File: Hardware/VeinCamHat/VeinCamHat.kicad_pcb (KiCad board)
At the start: 2 copper layers, 65 x 56 mm, 65 parts, among them J1 10118193-0001LF, J2 Raspberry_Pi_2_3, Q1 BSD235N, Q2 MMUN2133L, SW1 SS-12D07-VG 4, U1 MCP3021, U2 TPS61092, U3 MCP73871

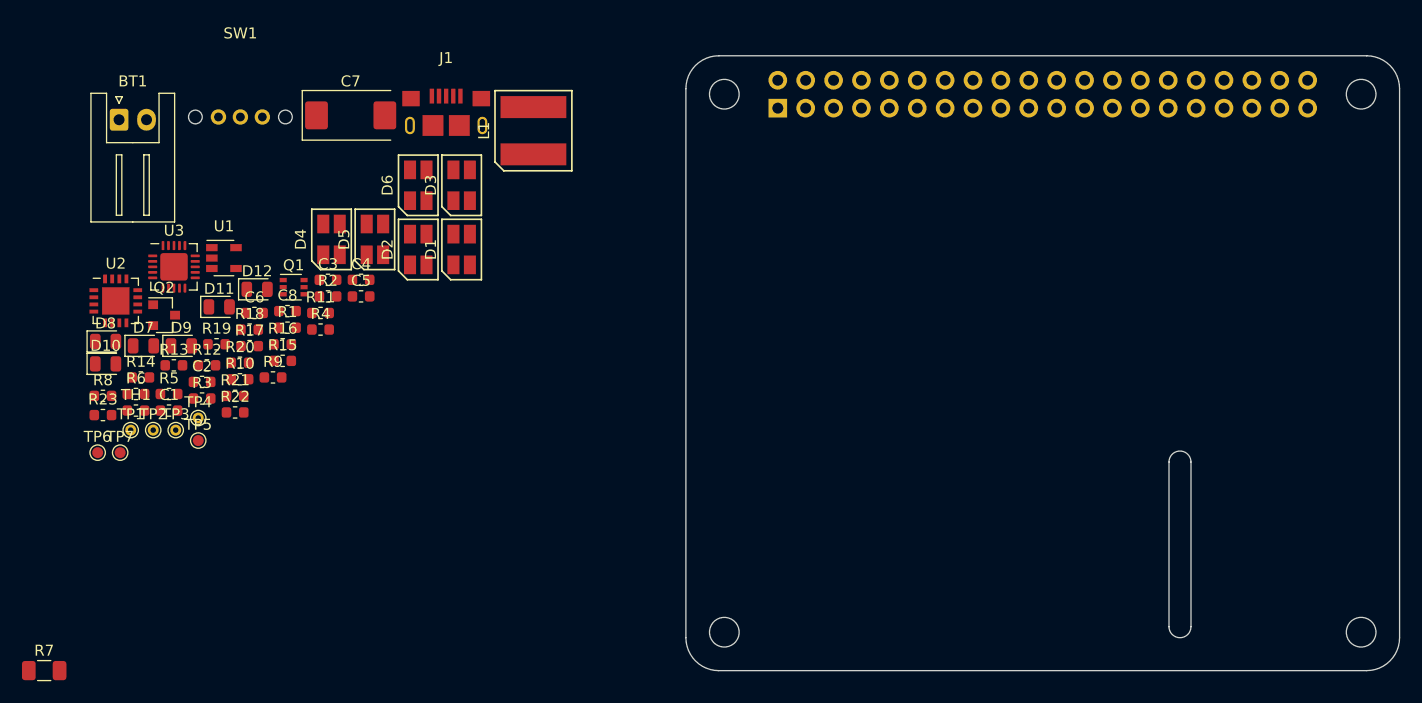
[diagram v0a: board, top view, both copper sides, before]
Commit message: Changed plans for VeinCam Plus, both boards laid out
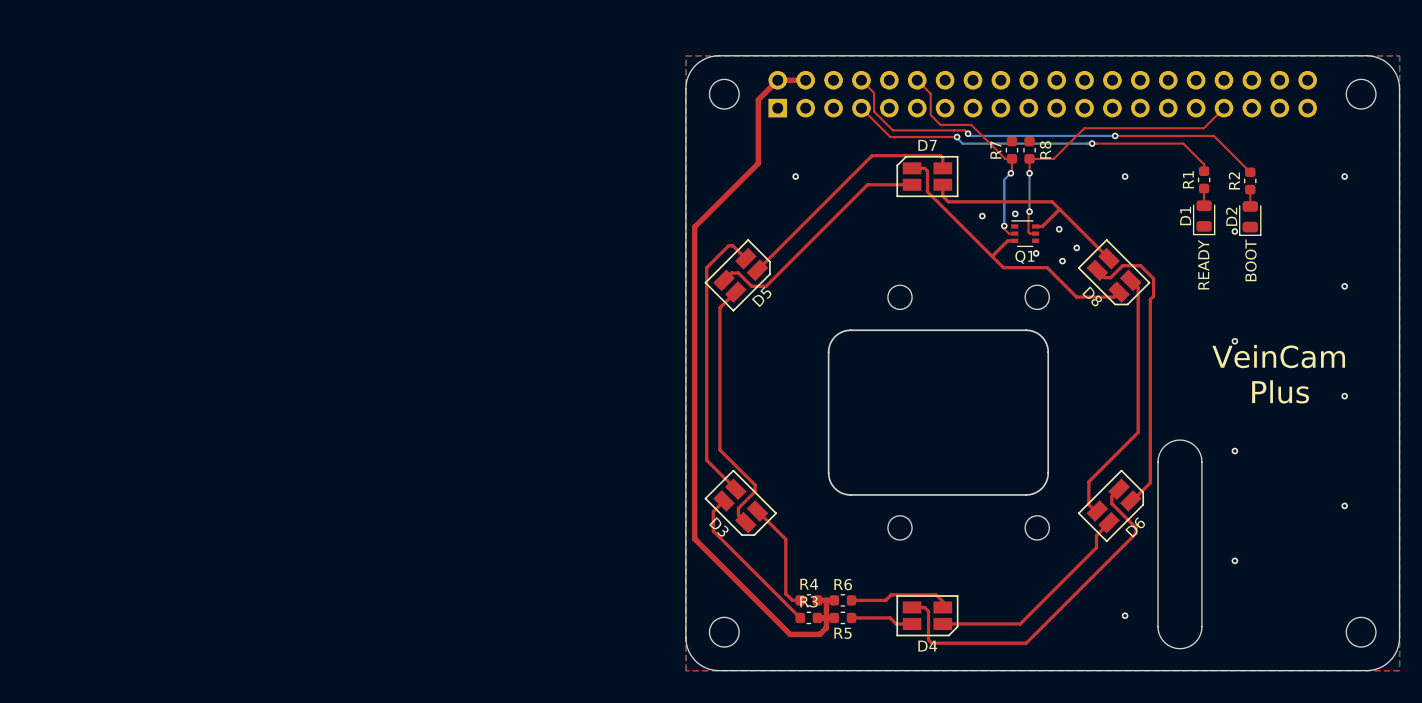
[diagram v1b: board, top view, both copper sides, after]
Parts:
- removed BT1: 3v7 LIPO, Connector_JST:JST_XH_S02B-XH-A_1x02_P2.50mm_Horizontal
- removed C1, C3, C4, C8: 10u, Capacitor_SMD:C_0603_1608Metric
- removed C2, C5: 100n, Capacitor_SMD:C_0603_1608Metric
- removed C6: 2u2, Capacitor_SMD:C_0603_1608Metric
- removed C7: 100u, Capacitor_Tantalum_SMD:CP_EIA-7343-31_Kemet-D
- removed D10, D12: RED LED, LED_SMD:LED_0805_2012Metric
- removed D11, D9: GREEN LED, LED_SMD:LED_0805_2012Metric
- removed J2: Raspberry_Pi_2_3, Connector_PinSocket_2.54mm:PinSocket_2x20_P2.54mm_Vertical
- removed L1: SRN6045-6R8Y, VeinCam_Footprints:SRN6045
- removed Q2: MMUN2133L, Package_TO_SOT_SMD:SOT-23
- removed R10, R14, R9: 10k, Resistor_SMD:R_0603_1608Metric
- removed R11, R12, R13, R15, R16, R21, R23: 1k, Resistor_SMD:R_0603_1608Metric
- removed R17: 1M87, Resistor_SMD:R_0603_1608Metric
- removed R18: 340k, Resistor_SMD:R_0603_1608Metric
- removed R19: 270k, Resistor_SMD:R_0603_1608Metric
- removed R20, R22: 100k, Resistor_SMD:R_0603_1608Metric
- removed SW1: SS-12D07-VG 4, VeinCam_Footprints:SS-12D07-VG4
- removed TH1: 10k NTC, Resistor_SMD:R_0603_1608Metric
- removed TP2, TP3, TP4: TestPoint, TestPoint:TestPoint_THTPad_D1.0mm_Drill0.5mm
- removed TP5: TP_BATT, TestPoint:TestPoint_Pad_D1.0mm
- removed TP6: TP_5V0, TestPoint:TestPoint_Pad_D1.0mm
- removed TP7: TP_VLIPO, TestPoint:TestPoint_Pad_D1.0mm
- removed U1: MCP3021, Package_TO_SOT_SMD:SOT-23-5
- removed U2: TPS61092, Package_DFN_QFN:QFN-16-1EP_4x4mm_P0.65mm_EP2.5x2.5mm
- removed U3: MCP73871, Package_DFN_QFN:QFN-20-1EP_4x4mm_P0.5mm_EP2.5x2.5mm
- D1: value SFH7252 -> GREEN LED; footprint VeinCam_Footprints:SFH7252 -> LED_SMD:LED_0805_2012Metric
- D2: value SFH7252 -> RED LED; footprint VeinCam_Footprints:SFH7252 -> LED_SMD:LED_0805_2012Metric
- D7: value GREEN LED -> SFH7252; footprint LED_SMD:LED_0805_2012Metric -> VeinCam_Footprints:SFH7252
- D8: value RED LED -> SFH7252; footprint LED_SMD:LED_0805_2012Metric -> VeinCam_Footprints:SFH7252
- J1: value 10118193-0001LF -> Raspberry_Pi_2_3; footprint VeinCam_Footprints:10118193-0001LF -> Connector_PinSocket_2.54mm:PinSocket_2x20_P2.54mm_Vertical; moved to B.Cu
- R1: value 0R0 -> 1k
- R2: value DNP -> 1k
- R7: value DNP -> 10k; footprint Resistor_SMD:R_1206_3216Metric -> Resistor_SMD:R_0603_1608Metric
- TP1: value TestPoint -> Camera Outline; footprint TestPoint:TestPoint_THTPad_D1.0mm_Drill0.5mm -> VeinCam_Footprints:PiCamera
- moved R7 100.1 mm to (229.7, 102.6), turned to 90 degrees
- moved D8 92.1 mm to (239.0, 114.0), turned to 45 degrees
- moved R8 87.3 mm to (231.3, 102.6), turned to 90 degrees
- moved R2 84.7 mm to (251.4, 105.4), turned to 270 degrees
- moved R1 84.6 mm to (247.2, 105.3), turned to 270 degrees
- moved D2 75.8 mm to (251.4, 108.7), turned to 90 degrees
- moved D7 73.1 mm to (222.0, 105.0), turned to 270 degrees
- moved TP1 72.6 mm to (222.0, 126.0), turned to 270 degrees
- moved D6 69.8 mm to (239.0, 135.0), turned to 135 degrees
- moved D1 67.7 mm to (247.2, 108.6), turned to 90 degrees
- moved R6 67.1 mm to (214.3, 143.6), turned to 180 degrees
- moved Q1 66.8 mm to (230.9, 110.2)
- moved R5 64.7 mm to (214.3, 145.2), turned to 180 degrees
- moved D4 64.2 mm to (222.0, 145.0), turned to 90 degrees
- moved R3 58.8 mm to (211.2, 145.2)
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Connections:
- D1 pad 1: Net-(D1-Pad1) -> GND
- D2 pad 1: Net-(D2-Pad1) -> GND
- D3 pad 2: Net-(D1-Pad1) -> Net-(D3-Pad2)
- D3 pad 4: Net-(D1-Pad3) -> Net-(D3-Pad4)
- D4 pad 2: Net-(D2-Pad1) -> Net-(D4-Pad2)
- D4 pad 4: Net-(D2-Pad3) -> Net-(D4-Pad4)
- D6 pad 1: Net-(D5-Pad1) -> Net-(D6-Pad1)
- D6 pad 3: Net-(D5-Pad3) -> Net-(D6-Pad3)
- D7 pad 1: GND -> Net-(D7-Pad1)
- D7 pad 2: Net-(D7-Pad2) -> Net-(D5-Pad1)
- D8 pad 1: GND -> Net-(D7-Pad1)
- D8 pad 2: Net-(D8-Pad2) -> Net-(D6-Pad1)
- J1 pad 1: VBUS -> (no net)
- J1 pad 2: (no net) -> +5V
- J1 pad 4: (no net) -> +5V
- J1 pad 5: GND -> (no net)
- Q1 pad 3: Net-(D5-Pad1) -> Net-(D7-Pad1)
- Q1 pad 6: Net-(D5-Pad3) -> Net-(D7-Pad3)
- R1 pad 1: +BATT -> /LED_READY
- R1 pad 2: Net-(R1-Pad2) -> Net-(D1-Pad2)
- R2 pad 1: Net-(R1-Pad2) -> /LED_BOOT
- R2 pad 2: GND -> Net-(D2-Pad2)
- R3 pad 1: Net-(D1-Pad2) -> Net-(D3-Pad2)
- R4 pad 1: Net-(D1-Pad4) -> Net-(D3-Pad4)
- R5 pad 1: Net-(D2-Pad2) -> Net-(D4-Pad2)
- R6 pad 1: Net-(D2-Pad4) -> Net-(D4-Pad4)
- R7 pad 1: +5V -> /LED_940
- R7 pad 2: VBUS -> GND
- R8 pad 1: +5V -> /LED_850
- R8 pad 2: /SCL -> GND
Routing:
- net +5V: track 0.00 -> 68.8 mm
- net /LED_BOOT: track 0.00 -> 39.9 mm, vias 0 -> 2
- net /LED_READY: track 0.00 -> 34.4 mm, vias 0 -> 2
- net Net-(D4-Pad3): track 0.00 -> 32.6 mm
- net Net-(D7-Pad1): track 0.00 -> 27.7 mm
- net Net-(D6-Pad1): track 0.00 -> 27.7 mm
- net /LED_850: track 0.00 -> 27.1 mm, vias 0 -> 2
- net Net-(D3-Pad3): track 0.00 -> 26.2 mm
- net Net-(D6-Pad3): track 0.00 -> 23.9 mm
- net Net-(D3-Pad1): track 0.00 -> 23.8 mm
- net Net-(D5-Pad1): track 0.00 -> 22.2 mm
- net Net-(D5-Pad3): track 0.00 -> 21.7 mm
- net Net-(D7-Pad3): track 0.00 -> 21.4 mm
- net /LED_940: track 0.00 -> 20.5 mm, vias 0 -> 2
- net Net-(D4-Pad1): track 0.00 -> 20.0 mm
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- added copper zone on B.Cu, net GND
- added copper zone on F.Cu, net GND
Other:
- outline, holes or cut-outs redrawn
- net class Default: via_dia 0.9 -> 0.6; via_drill 0.6 -> 0.3
- rule trace_min: 0.1524 -> 0.2
- rule via_min_drill: 0.5 -> 0.3
- rule via_min_size: 0.8 -> 0.6
- board text added: "BOOT"
- board text added: "READY"
- board text added: "VeinCam Plus"

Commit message: More Hardware changes, both boards complete
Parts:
- Q1: value BSD235N -> NTJD4001N
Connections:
- J1 pad 1: (no net) -> Net-(J1-Pad1)
- J1 pad 10: (no net) -> Net-(J1-Pad10)
- J1 pad 11: (no net) -> Net-(J1-Pad11)
- J1 pad 13: (no net) -> Net-(J1-Pad13)
- J1 pad 15: (no net) -> Net-(J1-Pad15)
- J1 pad 16: (no net) -> Net-(J1-Pad16)
- J1 pad 17: (no net) -> Net-(J1-Pad17)
- J1 pad 18: (no net) -> Net-(J1-Pad18)
- J1 pad 19: (no net) -> Net-(J1-Pad19)
- J1 pad 21: (no net) -> Net-(J1-Pad21)
- J1 pad 22: (no net) -> Net-(J1-Pad22)
- J1 pad 23: (no net) -> Net-(J1-Pad23)
- J1 pad 24: (no net) -> Net-(J1-Pad24)
- J1 pad 26: (no net) -> Net-(J1-Pad26)
- J1 pad 27: (no net) -> Net-(J1-Pad27)
- J1 pad 28: (no net) -> Net-(J1-Pad28)
- J1 pad 29: (no net) -> Net-(J1-Pad29)
- J1 pad 3: (no net) -> Net-(J1-Pad3)
- J1 pad 31: (no net) -> Net-(J1-Pad31)
- J1 pad 32: (no net) -> Net-(J1-Pad32)
- J1 pad 35: (no net) -> Net-(J1-Pad35)
- J1 pad 36: (no net) -> Net-(J1-Pad36)
- J1 pad 37: (no net) -> Net-(J1-Pad37)
- J1 pad 38: (no net) -> Net-(J1-Pad38)
- J1 pad 40: (no net) -> Net-(J1-Pad40)
- J1 pad 5: (no net) -> Net-(J1-Pad5)

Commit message: final board changes, gerbers generated
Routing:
- net GND: vias 17 -> 19
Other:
- rule solder_mask_min_width: 0.25 -> 0.1
- board text added: "Note: 1.6mm FR4"
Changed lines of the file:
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@@
   (general
     (thickness 1.6)
-    (drawings 17)
-    (tracks 177)
+    (drawings 18)
+    (tracks 179)
     (zones 0)
     (modules 23)
@@
     (pad_drill 2.5)
     (pad_to_mask_clearance 0)
-    (solder_mask_min_width 0.25)
+    (solder_mask_min_width 0.1)
     (aux_axis_origin 200 150)
     (visible_elements 7FFFF7FF)
     (pcbplotparams
-      (layerselection 0x00030_80000001)
+      (layerselection 0x012f8_ffffffff)
       (usegerberextensions true)
       (usegerberattributes false)
@@
       (outputformat 1)
       (mirror false)
-      (drillshape 1)
+      (drillshape 0)
       (scaleselection 1)
-      (outputdirectory ""))
+      (outputdirectory "gerbers/"))
   )
   (net 0 "")
@@
     (descr "Through hole straight socket strip, 2x20, 2.54mm pitch, double cols (from Kicad 4.0.7), script generated")
     (tags "Through hole socket strip THT 2x20 2.54mm double row")
-    (fp_text reference J1 (at -1.27 2.77 270) (layer B.SilkS)
+    (fp_text reference J1 (at -1.27 2.77 270) (layer B.Fab)
       (effects (font (size 1 1) (thickness 0.15)) (justify mirror))
     )
@@
       (rotate (xyz 90 -180 0))
     )
+  )
+  (gr_text "Note: 1.6mm FR4" (at 229.8 154) (layer Cmts.User)
+    (effects (font (size 1 1) (thickness 0.25)))
   )
   (gr_text "VeinCam\nPlus" (at 254.1 123.1) (layer F.SilkS)
@@
   (via (at 240 145) (size 0.6) (drill 0.3) (layers F.Cu B.Cu) (net 2))
   (via (at 210 105) (size 0.6) (drill 0.3) (layers F.Cu B.Cu) (net 2))
+  (via (at 207.4 148.1) (size 0.6) (drill 0.3) (layers F.Cu B.Cu) (net 2))
+  (via (at 219.4 148.3) (size 0.6) (drill 0.3) (layers F.Cu B.Cu) (net 2))
   (segment (start 247.2 106.0875) (end 247.2 107.6625) (width 0.2) (layer F.Cu) (net 3))
   (segment (start 251.4 106.1875) (end 251.4 107.725) (width 0.2) (layer F.Cu) (net 4))
@@
   (segment (start 218.6 145.2) (end 219.150001 145.750001) (width 0.3) (layer F.Cu) (net 18))
   (segment (start 240.649519 134.550481) (end 240.349519 134.550481) (width 0.3) (layer F.Cu) (net 19))
-  (segment (start 242.3 116.2) (end 242.3 132.9) (width 0.3) (layer F.Cu) (net 19))
-  (segment (start 242.6 115.9) (end 242.3 116.2) (width 0.3) (layer F.Cu) (net 19))
+  (segment (start 241.9 133.3) (end 240.649519 134.550481) (width 0.3) (layer F.Cu) (net 19))
+  (segment (start 242.6 115.9) (end 241.9 116.6) (width 0.3) (layer F.Cu) (net 19))
   (segment (start 237.47972 113.540381) (end 238.15147 114.212131) (width 0.3) (layer F.Cu) (net 19))
   (segment (start 238.687869 114.212131) (end 239.78034 113.11966) (width 0.3) (layer F.Cu) (net 19))
-  (segment (start 242.3 132.9) (end 240.649519 134.550481) (width 0.3) (layer F.Cu) (net 19))
+  (segment (start 241.9 116.6) (end 241.9 133.3) (width 0.3) (layer F.Cu) (net 19))
   (segment (start 239.78034 113.11966) (end 241.41966 113.11966) (width 0.3) (layer F.Cu) (net 19))
   (segment (start 241.41966 113.11966) (end 242.6 114.3) (width 0.3) (layer F.Cu) (net 19))
